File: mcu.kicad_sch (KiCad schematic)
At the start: 26 parts, among them J2 USB-C, J3 UART0, J4 I2C / Qwiic, J5 Spare IO, J6 Rail break-out, SW1 RESET, SW2 BOOT, U4 ESP32-S3-WROOM-1-N16R8, U5 USBLC6-2SC6

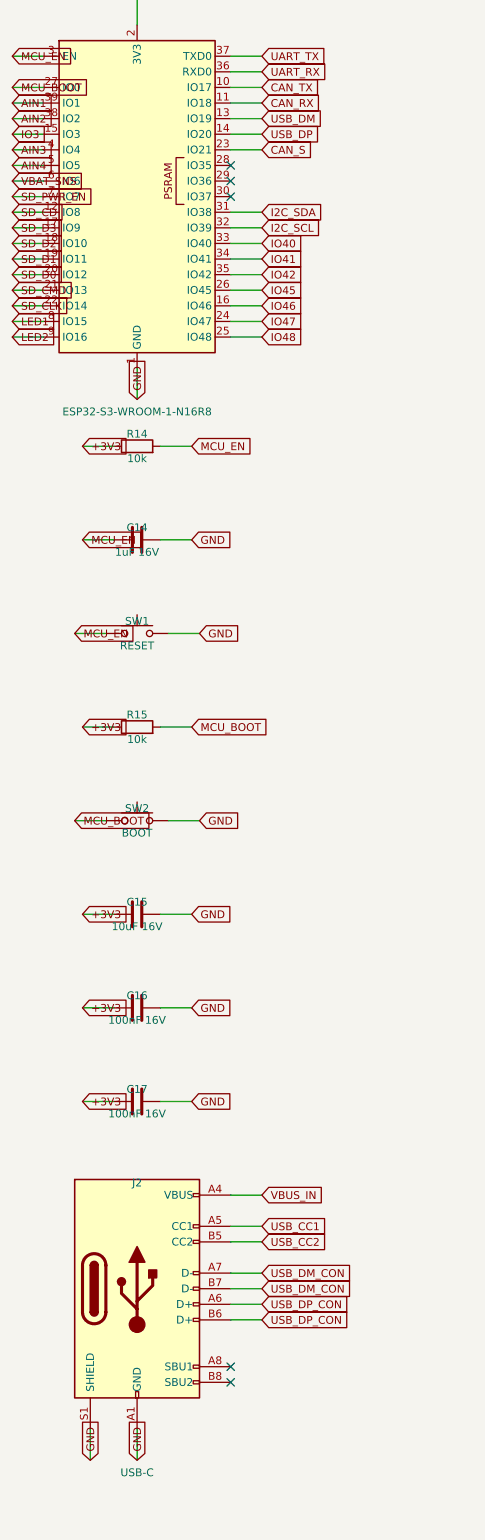
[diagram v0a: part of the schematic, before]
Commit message: Pass ERC clean on KiCad 9.0 and regenerate against its libraries
- Add a PWR_FLAG on VBAT_FB so the LM74700 ANODE power-input pin, fed
  through the reverse-battery FET and EMI bead, no longer trips
  power_pin_not_driven.
- Resolve the generic MOSFET symbols from Transistor_FET where the
  KiCad 9 libraries moved them out of Device.
- Handle the KiCad 9 library format in the raw-symbol extractor: tab
  indentation, CRLF line endings, and no trailing space after the
  symbol name.
- Flatten derived symbols the way KiCad does — carry the child's whole
  property blocks into the parent geometry instead of only swapping the
  value strings — so the embedded USBLC6-2SC6 matches the library copy.
- Regenerate all sheets, netlist, and the PDF plot; embedded symbol
  definitions now come from the KiCad 9.0 (20241209) libraries.

Validated with kicad-cli 9.0: all sheets load, connectivity matches
netlist.txt on 102 nets / 153 instances, ERC clean.

Co-Authored-By: Claude Fable 5 <noreply@anthropic.com>
Claude-Session: https://claude.ai/code/session_01DhNbL25h25p8VFCjRfJik9
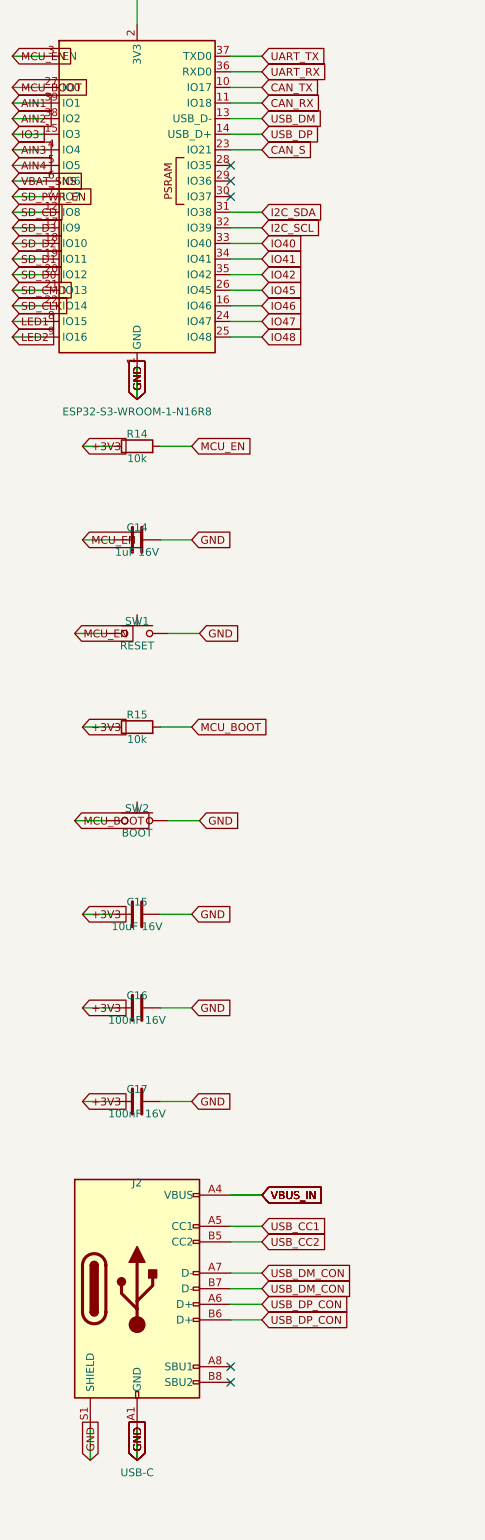
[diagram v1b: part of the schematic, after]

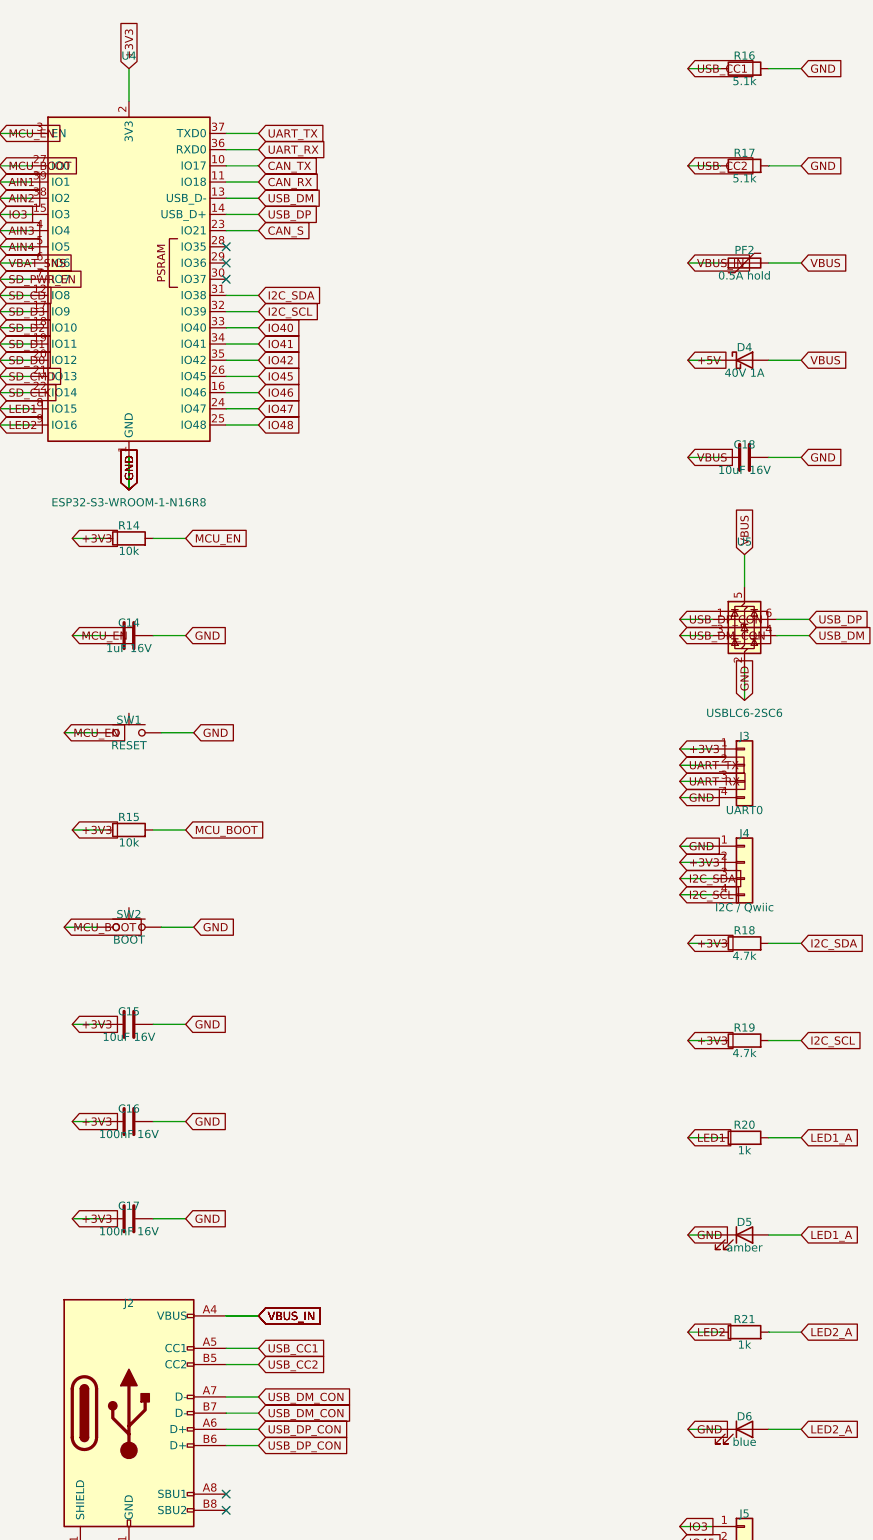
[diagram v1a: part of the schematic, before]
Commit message: Fix the LM5164 power stages against the datasheet and TI's DDA drawing
Review of datasheet SNVSAU4D and package drawing 4214849/B (DDA0008B)
caught five issues, all fixed and re-verified:

- RON placeholders (100k -> ~125/83kHz) corrected to 31.6k (396kHz, 5V)
  and 20.5k (402kHz, 3V3); minimum on-time at the 53.3V clamp is
  237ns/154ns, well above the 50ns floor.
- Bootstrap caps were 100nF; the datasheet mandates exactly 2.2nF and
  warns larger values damage the internal VCC regulator. Now 2.2nF 50V.
- No FB ripple injection on the all-ceramic outputs -- a COT stability
  requirement (Table 6-1). Added Type-3 networks (RA/CA/CB: 121k and
  95.3k / 3.3nF / 270pF) sized for ~20mV ramp at 14V per TI's example.
- Exposed-pad footprint EP2.41x3.3mm was smaller than the DDA0008B pad
  itself (max 2.71x3.4mm); swapped to the EP2.95x4.9mm_Mask2.71x3.4mm
  footprint matching TI's example land pattern.
- Quantified BAT54S back-feed into +3V3: one input shorted to battery
  floats the rail to ~3.6V when the MCU sleeps. Added D2, an MM3Z3V6T1G
  3.6V zener rail clamp.

Load-dump assumption confirmed by the owner: alternator never exceeds
20V, so the SMCJ33A standoff has comfortable margin.

Validated with kicad-cli 9.0: 104 nets / 160 instances match, ERC clean.

Co-Authored-By: Claude Fable 5 <noreply@anthropic.com>
Claude-Session: https://claude.ai/code/session_01DhNbL25h25p8VFCjRfJik9
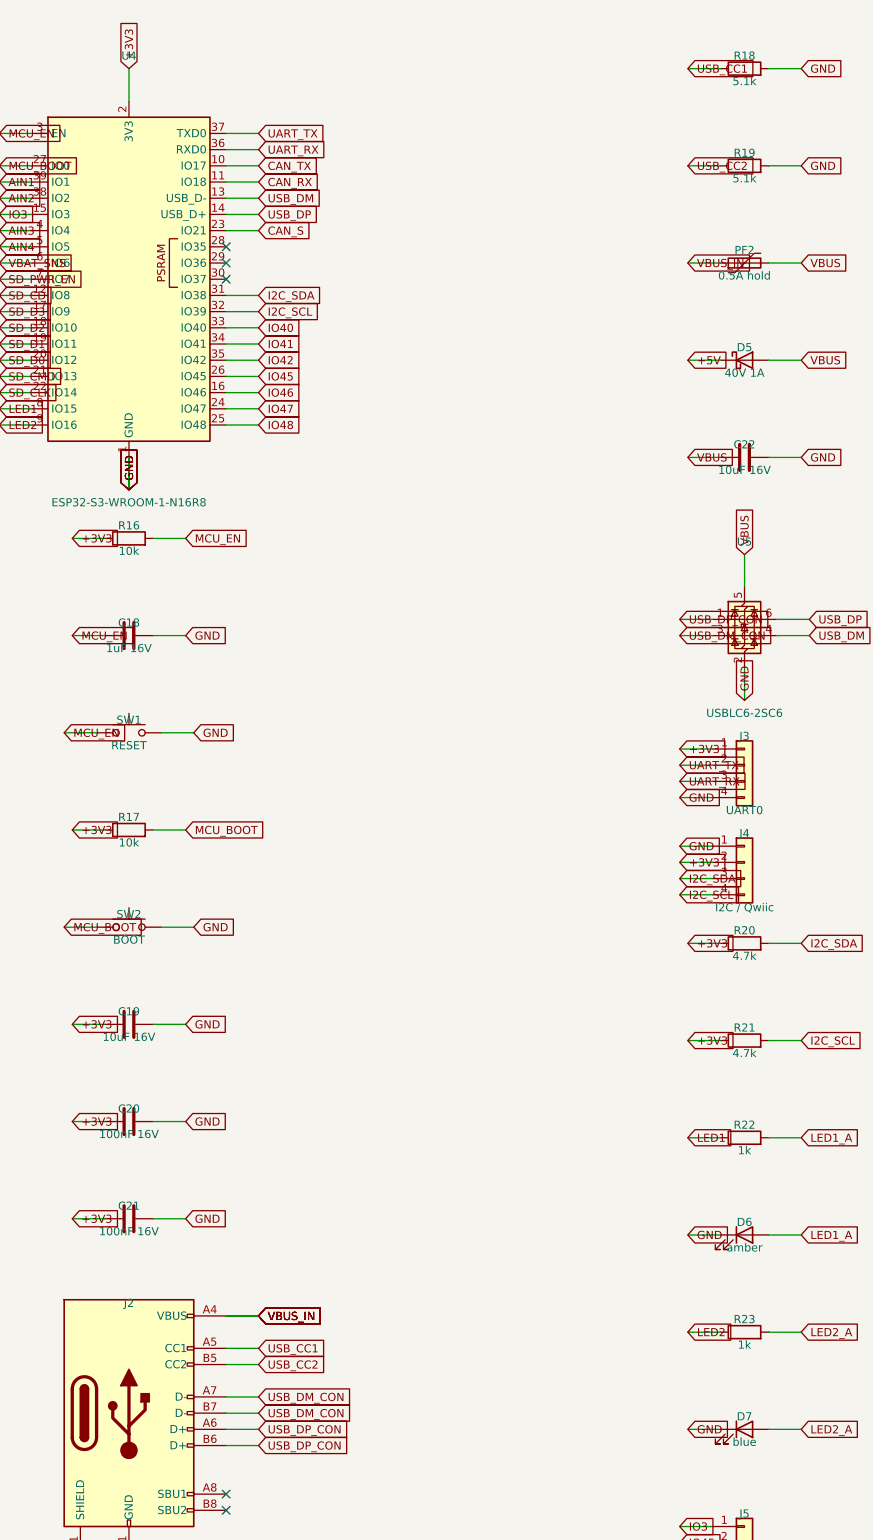
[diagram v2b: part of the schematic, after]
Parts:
- removed C14: 1uF 16V, Capacitor_SMD:C_0805_2012Metric, symbol Device:C
- removed C15: 10uF 16V, Capacitor_SMD:C_1206_3216Metric, symbol Device:C
- removed C16, C17: 100nF 16V, Capacitor_SMD:C_0805_2012Metric, symbol Device:C
- removed D4: 40V 1A, Diode_SMD:D_SOD-123, symbol Device:D_Schottky
- removed R14, R15: 10k, Resistor_SMD:R_0805_2012Metric, symbol Device:R
- added C19, C22: 10uF 16V, Capacitor_SMD:C_1206_3216Metric, symbol Device:C
- added C20, C21: 100nF 16V, Capacitor_SMD:C_0805_2012Metric, symbol Device:C
- added D7: blue, LED_SMD:LED_0805_2012Metric, symbol Device:LED
- added R22, R23: 1k, Resistor_SMD:R_0805_2012Metric, symbol Device:R
- C18: value 10uF 16V -> 1uF 16V; footprint Capacitor_SMD:C_1206_3216Metric -> Capacitor_SMD:C_0805_2012Metric; Note (none) -> EN reset delay
- D5: value amber -> 40V 1A; footprint LED_SMD:LED_0805_2012Metric -> Diode_SMD:D_SOD-123; symbol Device:LED -> Device:D_Schottky; MPN (none) -> PMEG4010; Note (none) -> OR-ing: bench USB can power the board, but the 5V buck (5.0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
- D6: value blue -> amber
- R16, R17: value 5.1k -> 10k
- R18, R19: value 4.7k -> 5.1k
- R20, R21: value 1k -> 4.7k
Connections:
- net +3V3: now also R16.1, R17.1, R20.1, R21.1, C19.1, C20.1, C21.1; no longer R18.1, R19.1
- net +5V: now also D5.1 (K)
- net GND: now also R18.2, R19.2, C19.2, C20.2, C21.2, C22.2, D7.1 (K); no longer D5.1 (K), R16.2, R17.2
- net I2C_SCL: now also R21.2; no longer R19.2
- net I2C_SDA: now also R20.2; no longer R18.2
- net LED1: now also R22.1; no longer R20.1
- net LED1_A: now also D6.2 (A), R22.2; no longer D5.2 (A), R20.2
- net LED2: now also R23.1; no longer R21.1
- net LED2_A: now also D7.2 (A), R23.2; no longer D6.2 (A), R21.2
- net MCU_BOOT: now also R17.2
- net MCU_EN: now also C18.1, R16.2
- net USB_CC1: now also R18.1; no longer R16.1
- net USB_CC2: now also R19.1; no longer R17.1
- net VBUS: now also D5.2 (A), C22.1; no longer C18.1
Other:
- moved on the sheet: C18, D6, R16, R17, R18, R19, R20, R21
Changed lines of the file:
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@@
   (symbol (lib_id "Device:R") (at 62.23 91.44 90) (unit 1)
     (in_bom yes) (on_board yes) (dnp no)
-    (property "Reference" "R14" (at 62.23 89.44 270)
+    (property "Reference" "R16" (at 62.23 89.44 270)
       (effects (font (size 1.27 1.27)) )
     )
@@
     (instances
       (project "esp32s3-can-sd-logger"
-        (path "/3276c6e6-7085-5954-8442-c6cef7eab316/a84bed91-088f-5303-a3fb-bbd35a494bf0" (reference "R14") (unit 1))
+        (path "/3276c6e6-7085-5954-8442-c6cef7eab316/a84bed91-088f-5303-a3fb-bbd35a494bf0" (reference "R16") (unit 1))
       )
     )
@@
   (symbol (lib_id "Device:C") (at 62.23 106.68 90) (unit 1)
     (in_bom yes) (on_board yes) (dnp no)
-    (property "Reference" "C14" (at 62.23 104.68 270)
+    (property "Reference" "C18" (at 62.23 104.68 270)
       (effects (font (size 1.27 1.27)) )
     )
@@
     (instances
       (project "esp32s3-can-sd-logger"
-        (path "/3276c6e6-7085-5954-8442-c6cef7eab316/a84bed91-088f-5303-a3fb-bbd35a494bf0" (reference "C14") (unit 1))
+        (path "/3276c6e6-7085-5954-8442-c6cef7eab316/a84bed91-088f-5303-a3fb-bbd35a494bf0" (reference "C18") (unit 1))
       )
     )
@@
   (symbol (lib_id "Device:R") (at 62.23 137.16 90) (unit 1)
     (in_bom yes) (on_board yes) (dnp no)
-    (property "Reference" "R15" (at 62.23 135.16 270)
+    (property "Reference" "R17" (at 62.23 135.16 270)
       (effects (font (size 1.27 1.27)) )
     )
@@
     (instances
       (project "esp32s3-can-sd-logger"
-        (path "/3276c6e6-7085-5954-8442-c6cef7eab316/a84bed91-088f-5303-a3fb-bbd35a494bf0" (reference "R15") (unit 1))
+        (path "/3276c6e6-7085-5954-8442-c6cef7eab316/a84bed91-088f-5303-a3fb-bbd35a494bf0" (reference "R17") (unit 1))
       )
     )
@@
   (symbol (lib_id "Device:C") (at 62.23 167.64 90) (unit 1)
     (in_bom yes) (on_board yes) (dnp no)
-    (property "Reference" "C15" (at 62.23 165.64 270)
+    (property "Reference" "C19" (at 62.23 165.64 270)
       (effects (font (size 1.27 1.27)) )
     )
@@
     (instances
       (project "esp32s3-can-sd-logger"
-        (path "/3276c6e6-7085-5954-8442-c6cef7eab316/a84bed91-088f-5303-a3fb-bbd35a494bf0" (reference "C15") (unit 1))
+        (path "/3276c6e6-7085-5954-8442-c6cef7eab316/a84bed91-088f-5303-a3fb-bbd35a494bf0" (reference "C19") (unit 1))
       )
     )
@@
   (symbol (lib_id "Device:C") (at 62.23 182.88 90) (unit 1)
     (in_bom yes) (on_board yes) (dnp no)
-    (property "Reference" "C16" (at 62.23 180.88 270)
+    (property "Reference" "C20" (at 62.23 180.88 270)
       (effects (font (size 1.27 1.27)) )
     )
@@
     (instances
       (project "esp32s3-can-sd-logger"
-        (path "/3276c6e6-7085-5954-8442-c6cef7eab316/a84bed91-088f-5303-a3fb-bbd35a494bf0" (reference "C16") (unit 1))
+        (path "/3276c6e6-7085-5954-8442-c6cef7eab316/a84bed91-088f-5303-a3fb-bbd35a494bf0" (reference "C20") (unit 1))
       )
     )
@@
   (symbol (lib_id "Device:C") (at 62.23 198.12 90) (unit 1)
     (in_bom yes) (on_board yes) (dnp no)
-    (property "Reference" "C17" (at 62.23 196.12 270)
+    (property "Reference" "C21" (at 62.23 196.12 270)
       (effects (font (size 1.27 1.27)) )
     )
@@
     (instances
       (project "esp32s3-can-sd-logger"
-        (path "/3276c6e6-7085-5954-8442-c6cef7eab316/a84bed91-088f-5303-a3fb-bbd35a494bf0" (reference "C17") (unit 1))
+        (path "/3276c6e6-7085-5954-8442-c6cef7eab316/a84bed91-088f-5303-a3fb-bbd35a494bf0" (reference "C21") (unit 1))
       )
     )
@@
   (symbol (lib_id "Device:R") (at 158.75 17.78 90) (unit 1)
     (in_bom yes) (on_board yes) (dnp no)
-    (property "Reference" "R16" (at 158.75 15.78 270)
+    (property "Reference" "R18" (at 158.75 15.78 270)
       (effects (font (size 1.27 1.27)) )
     )
@@
     (instances
       (project "esp32s3-can-sd-logger"
-        (path "/3276c6e6-7085-5954-8442-c6cef7eab316/a84bed91-088f-5303-a3fb-bbd35a494bf0" (reference "R16") (unit 1))
+        (path "/3276c6e6-7085-5954-8442-c6cef7eab316/a84bed91-088f-5303-a3fb-bbd35a494bf0" (reference "R18") (unit 1))
       )
     )
@@
   (symbol (lib_id "Device:R") (at 158.75 33.02 90) (unit 1)
     (in_bom yes) (on_board yes) (dnp no)
-    (property "Reference" "R17" (at 158.75 31.02 270)
+    (property "Reference" "R19" (at 158.75 31.02 270)
       (effects (font (size 1.27 1.27)) )
     )
@@
     (instances
       (project "esp32s3-can-sd-logger"
-        (path "/3276c6e6-7085-5954-8442-c6cef7eab316/a84bed91-088f-5303-a3fb-bbd35a494bf0" (reference "R17") (unit 1))
+        (path "/3276c6e6-7085-5954-8442-c6cef7eab316/a84bed91-088f-5303-a3fb-bbd35a494bf0" (reference "R19") (unit 1))
       )
     )
@@
   (symbol (lib_id "Device:D_Schottky") (at 158.75 63.5 0) (unit 1)
     (in_bom yes) (on_board yes) (dnp no)
-    (property "Reference" "D4" (at 158.75 61.5 0)
+    (property "Reference" "D5" (at 158.75 61.5 0)
       (effects (font (size 1.27 1.27)) )
     )
@@
     (instances
       (project "esp32s3-can-sd-logger"
-        (path "/3276c6e6-7085-5954-8442-c6cef7eab316/a84bed91-088f-5303-a3fb-bbd35a494bf0" (reference "D4") (unit 1))
+        (path "/3276c6e6-7085-5954-8442-c6cef7eab316/a84bed91-088f-5303-a3fb-bbd35a494bf0" (reference "D5") (unit 1))
       )
     )
@@
   (symbol (lib_id "Device:C") (at 158.75 78.74 90) (unit 1)
     (in_bom yes) (on_board yes) (dnp no)
-    (property "Reference" "C18" (at 158.75 76.74 270)
+    (property "Reference" "C22" (at 158.75 76.74 270)
       (effects (font (size 1.27 1.27)) )
     )
@@
     (instances
       (project "esp32s3-can-sd-logger"
-        (path "/3276c6e6-7085-5954-8442-c6cef7eab316/a84bed91-088f-5303-a3fb-bbd35a494bf0" (reference "C18") (unit 1))
+        (path "/3276c6e6-7085-5954-8442-c6cef7eab316/a84bed91-088f-5303-a3fb-bbd35a494bf0" (reference "C22") (unit 1))
       )
     )
@@
   (symbol (lib_id "Device:R") (at 158.75 154.94 90) (unit 1)
     (in_bom yes) (on_board yes) (dnp no)
-    (property "Reference" "R18" (at 158.75 152.94 270)
+    (property "Reference" "R20" (at 158.75 152.94 270)
       (effects (font (size 1.27 1.27)) )
     )
@@
     (instances
       (project "esp32s3-can-sd-logger"
-        (path "/3276c6e6-7085-5954-8442-c6cef7eab316/a84bed91-088f-5303-a3fb-bbd35a494bf0" (reference "R18") (unit 1))
+        (path "/3276c6e6-7085-5954-8442-c6cef7eab316/a84bed91-088f-5303-a3fb-bbd35a494bf0" (reference "R20") (unit 1))
       )
     )
@@
   (symbol (lib_id "Device:R") (at 158.75 170.18 90) (unit 1)
     (in_bom yes) (on_board yes) (dnp no)
-    (property "Reference" "R19" (at 158.75 168.18 270)
+    (property "Reference" "R21" (at 158.75 168.18 270)
       (effects (font (size 1.27 1.27)) )
     )
@@
     (instances
       (project "esp32s3-can-sd-logger"
-        (path "/3276c6e6-7085-5954-8442-c6cef7eab316/a84bed91-088f-5303-a3fb-bbd35a494bf0" (reference "R19") (unit 1))
+        (path "/3276c6e6-7085-5954-8442-c6cef7eab316/a84bed91-088f-5303-a3fb-bbd35a494bf0" (reference "R21") (unit 1))
       )
     )
@@
   (symbol (lib_id "Device:R") (at 158.75 185.42 90) (unit 1)
     (in_bom yes) (on_board yes) (dnp no)
-    (property "Reference" "R20" (at 158.75 183.42 270)
+    (property "Reference" "R22" (at 158.75 183.42 270)
       (effects (font (size 1.27 1.27)) )
     )
@@
     (instances
       (project "esp32s3-can-sd-logger"
-        (path "/3276c6e6-7085-5954-8442-c6cef7eab316/a84bed91-088f-5303-a3fb-bbd35a494bf0" (reference "R20") (unit 1))
+        (path "/3276c6e6-7085-5954-8442-c6cef7eab316/a84bed91-088f-5303-a3fb-bbd35a494bf0" (reference "R22") (unit 1))
       )
     )
@@
   (symbol (lib_id "Device:LED") (at 158.75 200.66 0) (unit 1)
     (in_bom yes) (on_board yes) (dnp no)
-    (property "Reference" "D5" (at 158.75 198.66 0)
+    (property "Reference" "D6" (at 158.75 198.66 0)
       (effects (font (size 1.27 1.27)) )
     )
@@
     (instances
       (project "esp32s3-can-sd-logger"
-        (path "/3276c6e6-7085-5954-8442-c6cef7eab316/a84bed91-088f-5303-a3fb-bbd35a494bf0" (reference "D5") (unit 1))
+        (path "/3276c6e6-7085-5954-8442-c6cef7eab316/a84bed91-088f-5303-a3fb-bbd35a494bf0" (reference "D6") (unit 1))
       )
     )
@@
   (symbol (lib_id "Device:R") (at 158.75 215.9 90) (unit 1)
     (in_bom yes) (on_board yes) (dnp no)
-    (property "Reference" "R21" (at 158.75 213.9 270)
+    (property "Reference" "R23" (at 158.75 213.9 270)
       (effects (font (size 1.27 1.27)) )
     )
@@
     (instances
       (project "esp32s3-can-sd-logger"
-        (path "/3276c6e6-7085-5954-8442-c6cef7eab316/a84bed91-088f-5303-a3fb-bbd35a494bf0" (reference "R21") (unit 1))
+        (path "/3276c6e6-7085-5954-8442-c6cef7eab316/a84bed91-088f-5303-a3fb-bbd35a494bf0" (reference "R23") (unit 1))
       )
     )
@@
   (symbol (lib_id "Device:LED") (at 158.75 231.14 0) (unit 1)
     (in_bom yes) (on_board yes) (dnp no)
-    (property "Reference" "D6" (at 158.75 229.14 0)
+    (property "Reference" "D7" (at 158.75 229.14 0)
       (effects (font (size 1.27 1.27)) )
     )
@@
     (instances
       (project "esp32s3-can-sd-logger"
-        (path "/3276c6e6-7085-5954-8442-c6cef7eab316/a84bed91-088f-5303-a3fb-bbd35a494bf0" (reference "D6") (unit 1))
-      )
-    )
+        (path "/3276c6e6-7085-5954-8442-c6cef7eab316/a84bed91-088f-5303-a3fb-bbd35a494bf0" (reference "D7") (unit 1))
+      )
+    )
